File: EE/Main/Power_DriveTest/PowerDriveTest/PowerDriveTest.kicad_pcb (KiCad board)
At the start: 2 copper layers, 28.5 x 31 mm, 26 parts, among them J1 TAG_CONNECT, J2 Conn_01x02_Pin, J3 Conn_01x05_Pin, U1 LM3670MF-3.3, U2 SN74LVC1T45DBV, U3 STM32F030F4Px, U4 MCP1640Cx-xCHY

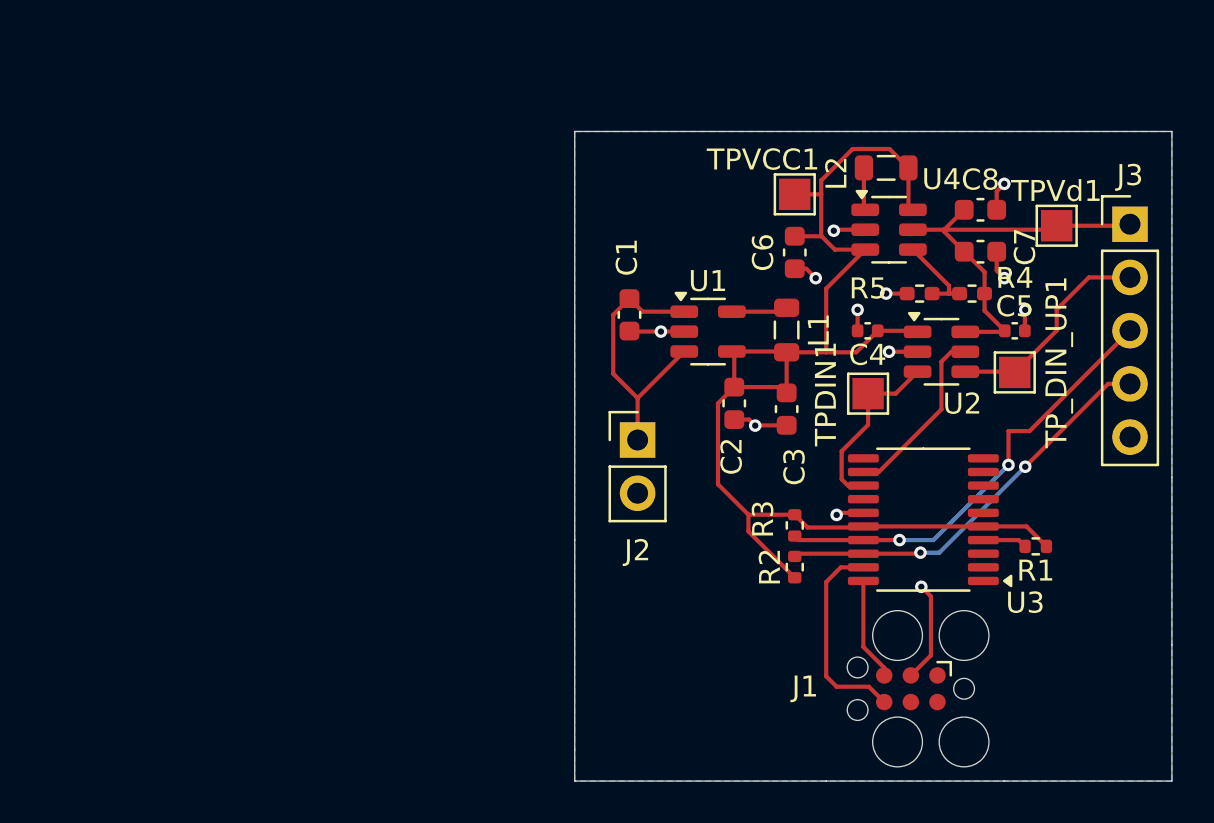
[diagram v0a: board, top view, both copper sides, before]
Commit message: New Power Board off to mfging
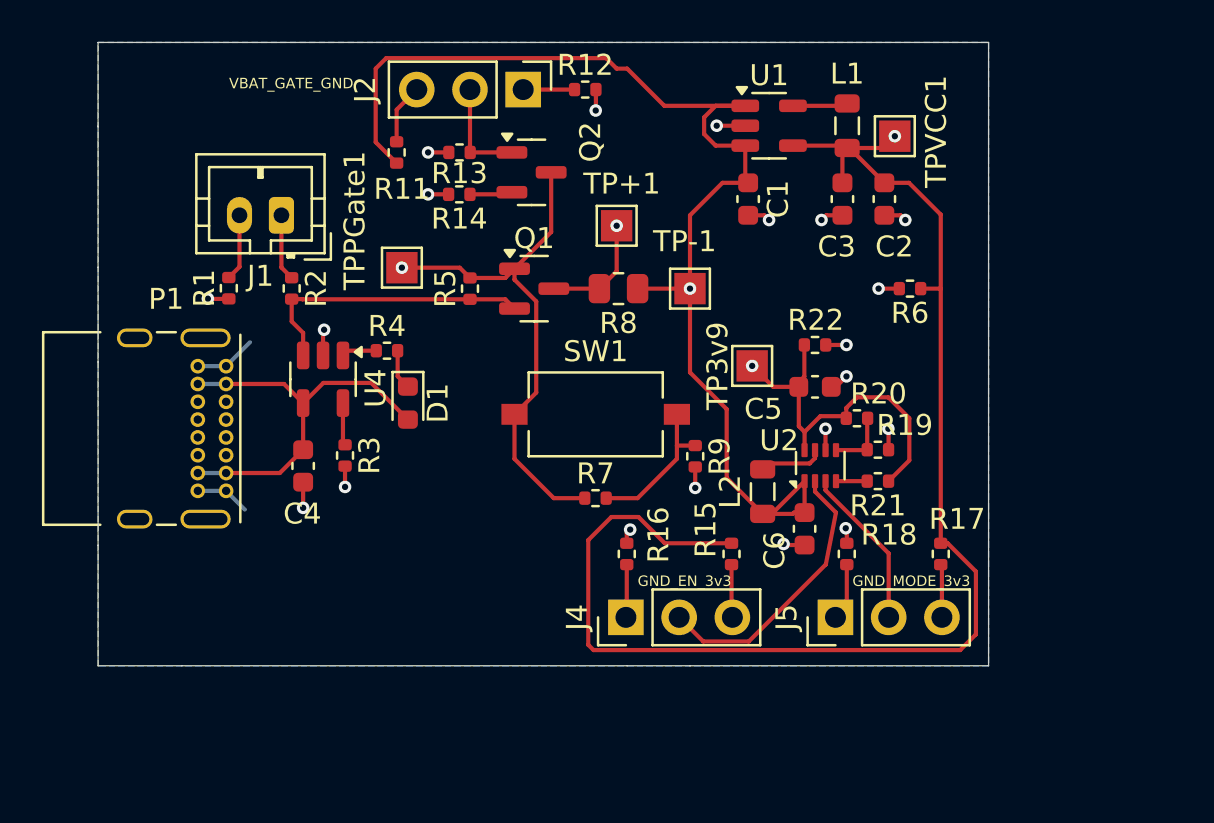
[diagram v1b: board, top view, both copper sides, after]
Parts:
- removed C7, C8: 4.7u, Capacitor_SMD:C_0603_1608Metric
- removed J3: Conn_01x05_Pin, Connector_PinHeader_2.54mm:PinHeader_1x05_P2.54mm_Vertical
- removed TPDIN1, TPVd1, TP_DIN_UP1: TestPoint, TestPoint:TestPoint_Pad_1.5x1.5mm
- removed U3: STM32F030F4Px, Package_SO:TSSOP-20_4.4x6.5mm_P0.65mm
- added D1: LED, LED_SMD:LED_0603_1608Metric, F.Cu at (148.0, 84.5)
- added J4: Conn_01x03_Pin, Connector_PinHeader_2.54mm:PinHeader_1x03_P2.54mm_Vertical, F.Cu at (158.4, 94.7)
- added J5: Conn_01x03_Pin, Connector_PinHeader_2.54mm:PinHeader_1x03_P2.54mm_Vertical, F.Cu at (168.4, 94.7)
- added P1: USB_C_Plug_USB2.0, Connector_USB:USB_C_Receptacle_GCT_USB4085, F.Cu at (139.4, 82.7)
- added Q1: Q_PMOS_GSD, Package_TO_SOT_SMD:SOT-23, F.Cu at (154.1, 79.0)
- added Q2: Q_NMOS_GSD, Package_TO_SOT_SMD:SOT-23, F.Cu at (153.9, 73.5)
- added R11: 10K, Resistor_SMD:R_0402_1005Metric, F.Cu at (147.5, 72.5)
- added R12: 10k, Resistor_SMD:R_0402_1005Metric, F.Cu at (156.5, 69.5)
- added R13: 10k, Resistor_SMD:R_0402_1005Metric, F.Cu at (150.5, 72.5)
- added R14: 10k, Resistor_SMD:R_0402_1005Metric, F.Cu at (150.5, 74.5)
- added R15: 10K, Resistor_SMD:R_0402_1005Metric, F.Cu at (163.5, 91.7)
- added R16: 10k, Resistor_SMD:R_0402_1005Metric, F.Cu at (158.5, 91.7)
- added R17: 10K, Resistor_SMD:R_0402_1005Metric, F.Cu at (173.5, 91.7)
- added R18: 10k, Resistor_SMD:R_0402_1005Metric, F.Cu at (169.0, 91.7)
- added R19: 100k, Resistor_SMD:R_0402_1005Metric, F.Cu at (170.5, 86.7)
- added R20: 550k, Resistor_SMD:R_0402_1005Metric, F.Cu at (169.5, 85.2)
- added R21: 10k, Resistor_SMD:R_0402_1005Metric, F.Cu at (170.5, 88.2)
- added R22: 1M, Resistor_SMD:R_0402_1005Metric, F.Cu at (167.5, 81.7)
- added R6: 1M, Resistor_SMD:R_0402_1005Metric, F.Cu at (172.0, 79.0)
- added R7: 0, Resistor_SMD:R_0402_1005Metric, F.Cu at (157.0, 89.0)
- added R8: 250m, Resistor_SMD:R_0805_2012Metric, F.Cu at (158.1, 79.0)
- added R9: 10k, Resistor_SMD:R_0402_1005Metric, F.Cu at (161.8, 87.0)
- added SW1: SW_SPST, Button_Switch_SMD:SW_Tactile_SPST_NO_Straight_CK_PTS636Sx25SMTRLFS, F.Cu at (157.0, 85.0)
- added TP+1: TestPoint, TestPoint:TestPoint_Pad_1.5x1.5mm, F.Cu at (158.0, 76.0)
- added TP-1: TestPoint, TestPoint:TestPoint_Pad_1.5x1.5mm, F.Cu at (161.5, 79.0)
- added TP3v9: TestPoint, TestPoint:TestPoint_Pad_1.5x1.5mm, F.Cu at (164.5, 82.7)
- added TPPGate1: TestPoint, TestPoint:TestPoint_Pad_1.5x1.5mm, F.Cu at (147.8, 78.0)
- C4, C5: value 0.1u -> 4.7u; footprint Capacitor_SMD:C_0402_1005Metric -> Capacitor_SMD:C_0603_1608Metric
- J1: value TAG_CONNECT -> Conn_01x02_Male; footprint Connector:Tag-Connect_TC2030-IDC-FP_2x03_P1.27mm_Vertical -> Connector_JST:JST_PH_B2B-PH-K_1x02_P2.00mm_Vertical
- J2: value Conn_01x02_Pin -> Conn_01x03_Pin; footprint Connector_PinHeader_2.54mm:PinHeader_1x02_P2.54mm_Vertical -> Connector_PinHeader_2.54mm:PinHeader_1x03_P2.54mm_Vertical
- L2: value 4.7u -> 0.47u
- R1: value 10k -> 0
- R2: value 4.7k -> 0
- R3: value 4.7k -> 10k
- R4: value 422k -> 2k; footprint Resistor_SMD:R_0402_1005Metric_Pad0.72x0.64mm_HandSolder -> Resistor_SMD:R_0402_1005Metric
- R5: value 250k -> 1M; footprint Resistor_SMD:R_0402_1005Metric_Pad0.72x0.64mm_HandSolder -> Resistor_SMD:R_0402_1005Metric
- U2: value SN74LVC1T45DBV -> ~; footprint Package_TO_SOT_SMD:SOT-23-6 -> Package_TO_SOT_SMD:SOT-583-8
- U4: value MCP1640Cx-xCHY -> MCP73832-2-OT; footprint Package_TO_SOT_SMD:SOT-23-6 -> Package_TO_SOT_SMD:SOT-23-5
- moved R1 40.4 mm to (139.5, 79.0), turned to 90 degrees
- moved J1 37.6 mm to (142.0, 75.5)
- moved R4 28.1 mm to (147.0, 82.0), turned to 0 degrees
- moved U4 27.9 mm to (144.0, 83.3), turned to -90 degrees
- moved C4 27.7 mm to (143.0, 87.5), turned to -90 degrees
- moved R2 27.4 mm to (142.5, 79.0), turned to -90 degrees
- moved R3 21.7 mm to (145.0, 87.0)
- moved R5 21.5 mm to (151.0, 79.0), turned to 90 degrees
- moved J2 17.6 mm to (153.5, 69.5), turned to -90 degrees
- moved L2 16.5 mm to (165.0, 88.7), turned to 90 degrees
- moved C6 13.2 mm to (167.0, 90.5), turned to 90 degrees
- moved C2 12.1 mm to (170.8, 74.7)
- moved C3 10.4 mm to (168.8, 74.7)
- moved U1 10.2 mm to (165.3, 71.2)
- moved L1 10.2 mm to (169.0, 71.2)
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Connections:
- C1 pad 1: /4v2 -> /VBAT_OUT
- C2 pad 1: VCC -> +3V3
- C3 pad 1: VCC -> +3V3
- C4 pad 1: VCC -> VBUS
- C5 pad 1: Vdrive -> /3v9
- C6 pad 1: VCC -> GND
- C6 pad 2: GND -> /VBAT_OUT
- J1 pad 1: unconnected-(J1-POWER_3V3-Pad1) -> Net-(J1-Pin_1)
- J1 pad 2: unconnected-(J1-UART_TX-Pad2) -> Net-(J1-Pin_2)
- J2 pad 1: /4v2 -> Net-(J2-Pin_1)
- J2 pad 2: GND -> /N_GATE
- L1 pad 2: VCC -> +3V3
- L2 pad 1: VCC -> /VBAT_OUT
- L2 pad 2: Net-(U4-SW) -> Net-(U2-SW)
- R1 pad 1: VCC -> GND
- R1 pad 2: Net-(U3-NRST) -> Net-(J1-Pin_2)
- R2 pad 1: VCC -> Net-(J1-Pin_1)
- R2 pad 2: /SDA -> /VBAT
- R3 pad 1: VCC -> Net-(U4-PROG)
- R3 pad 2: /SCL -> GND
- R4 pad 1: Vdrive -> Net-(U4-STAT)
- R4 pad 2: Net-(U4-V_{FB}) -> Net-(D1-K)
- R5 pad 1: Net-(U4-V_{FB}) -> /VBAT
- R5 pad 2: GND -> /GATE_EN
- TPVCC1 pad 1: VCC -> +3V3
- U1 pad 1: /4v2 -> /VBAT_OUT
- U1 pad 3: /4v2 -> /VBAT_OUT
- U1 pad 4: VCC -> +3V3
- U2 pad 1: VCC -> /VBAT_OUT
- U2 pad 2: GND -> /EN
- U2 pad 3: /DISPLAY_DIN -> /MODE
- U2 pad 4: /DISPLAY_DOUT -> Net-(U2-PG)
- U2 pad 5: /DIR -> Net-(U2-FB)
- U2 pad 6: Vdrive -> GND
- U4 pad 1: Net-(U4-SW) -> Net-(U4-STAT)
- U4 pad 3: VCC -> /VBAT
- U4 pad 4: Net-(U4-V_{FB}) -> VBUS
- U4 pad 5: Vdrive -> Net-(U4-PROG)
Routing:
- net +3V3: track 0.00 -> 66.3 mm, vias 0 -> 1
- net VCC: track 61.9 -> 0.00 mm
- net /VBAT_OUT: track 0.00 -> 58.5 mm, vias 0 -> 1
- net /GATE_EN: track 0.00 -> 25.2 mm, vias 0 -> 1
- net /SCL: track 21.2 -> 0.00 mm, vias 2 -> 0
- net Vdrive: track 19.7 -> 0.00 mm
- net /SDA: track 19.4 -> 0.00 mm, vias 2 -> 0
- net VBUS: track 0.00 -> 19.2 mm
- net /3v9: track 0.00 -> 17.8 mm, vias 0 -> 1
- net /VBAT: track 0.00 -> 13.8 mm
- net /4v2: track 13.6 -> 0.00 mm
- net /EN: track 0.00 -> 13.4 mm
- net /DISPLAY_DOUT: track 10.3 -> 0.00 mm
- net /SWDIO: track 9.84 -> 0.00 mm
- net /DIR: track 8.57 -> 0.00 mm
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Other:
- board size 28.5 x 31 mm -> 42.5 x 29.8 mm
- board text added: "GND_EN_3v3"
- board text added: "GND_MODE_3v3"
- board text added: "VBAT_GATE_GND"

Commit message: Placement Update
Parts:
- removed C3, C5: 4.7u, Capacitor_SMD:C_0603_1608Metric
- removed J1: Conn_01x02_Male, Connector_JST:JST_PH_B2B-PH-K_1x02_P2.00mm_Vertical
- removed J2, J4, J5: Conn_01x03_Pin, Connector_PinHeader_2.54mm:PinHeader_1x03_P2.54mm_Vertical
- removed L1: 4.7u, Inductor_SMD:L_0805_2012Metric
- removed R17: 10K, Resistor_SMD:R_0402_1005Metric
- removed R18, R21: 10k, Resistor_SMD:R_0402_1005Metric
- removed R19: 100k, Resistor_SMD:R_0402_1005Metric
- removed R22: 1M, Resistor_SMD:R_0402_1005Metric
- removed TP3v9: TestPoint, TestPoint:TestPoint_Pad_1.5x1.5mm
- removed U4: MCP73832-2-OT, Package_TO_SOT_SMD:SOT-23-5
- added C7: 0.1u, Capacitor_SMD:C_0402_1005Metric, F.Cu at (107.0, 101.3)
- added C8: 4.7u, Capacitor_SMD:C_0603_1608Metric, F.Cu at (121.6, 95.9)
- added C9: 0.1u, Capacitor_SMD:C_0402_1005Metric, F.Cu at (107.0, 103.2)
- added D2: LED, LED_SMD:LED_0603_1608Metric, F.Cu at (120.9, 79.0)
- added J7: TAG_CONNECT, Connector:Tag-Connect_TC2030-IDC-FP_2x03_P1.27mm_Vertical, F.Cu at (122.5, 24.9)
- added J8: Conn_01x02_Male, Connector_JST:JST_PH_B2B-PH-K_1x02_P2.00mm_Vertical, F.Cu at (100.6, 101.0)
- added Q3: Q_NMOS_GSD, Package_TO_SOT_SMD:SOT-23, F.Cu at (95.2, 86.8)
- added Q4: Q_NMOS_GSD, Package_TO_SOT_SMD:SOT-23, F.Cu at (95.2, 91.4)
- added R10: 10k, Resistor_SMD:R_0402_1005Metric_Pad0.72x0.64mm_HandSolder, F.Cu at (102.5, 82.1)
- added U3: 74LVC1GU04DRL, Package_TO_SOT_SMD:SOT-553, F.Cu at (121.1, 81.8)
- added U5: LM3670MF-3.3, Package_TO_SOT_SMD:TSOT-23-5, F.Cu at (120.9, 105.0)
- C1: value 4.7u -> 0.1u; footprint Capacitor_SMD:C_0603_1608Metric -> Capacitor_SMD:C_0402_1005Metric
- L2: value 0.47u -> 4.7u
- R1, R2: value 0 -> 100k; footprint Resistor_SMD:R_0402_1005Metric -> Resistor_SMD:R_0402_1005Metric_Pad0.72x0.64mm_HandSolder
- R11: value 10K -> 0; footprint Resistor_SMD:R_0402_1005Metric -> Resistor_SMD:R_0402_1005Metric_Pad0.72x0.64mm_HandSolder
- R12: value 10k -> 25m; footprint Resistor_SMD:R_0402_1005Metric -> Resistor_SMD:R_0805_2012Metric_Pad1.20x1.40mm_HandSolder
- R13, R9: value 10k -> 100k; footprint Resistor_SMD:R_0402_1005Metric -> Resistor_SMD:R_0402_1005Metric_Pad0.72x0.64mm_HandSolder
- R14, R15, R16, R3, R6, R7: footprint Resistor_SMD:R_0402_1005Metric -> Resistor_SMD:R_0402_1005Metric_Pad0.72x0.64mm_HandSolder
- R20: value 550k -> 4.7k; footprint Resistor_SMD:R_0402_1005Metric -> Resistor_SMD:R_0402_1005Metric_Pad0.72x0.64mm_HandSolder
- R4: value 2k -> 10k; footprint Resistor_SMD:R_0402_1005Metric -> Resistor_SMD:R_0402_1005Metric_Pad0.72x0.64mm_HandSolder
- R5: value 1M -> 4.7k; footprint Resistor_SMD:R_0402_1005Metric -> Resistor_SMD:R_0402_1005Metric_Pad0.72x0.64mm_HandSolder
- R8: value 250m -> 10; footprint Resistor_SMD:R_0805_2012Metric -> Resistor_SMD:R_0402_1005Metric_Pad0.72x0.64mm_HandSolder
- SW1: value SW_SPST -> SW_DPST; footprint Button_Switch_SMD:SW_Tactile_SPST_NO_Straight_CK_PTS636Sx25SMTRLFS -> Library:401-1133-ND
- U1: value LM3670MF-3.3 -> STM32G431K6Tx; footprint Package_TO_SOT_SMD:TSOT-23-5 -> Package_QFP:LQFP-32_7x7mm_P0.8mm
- U2: value ~ -> MCP73832-2-OT; footprint Package_TO_SOT_SMD:SOT-583-8 -> Package_TO_SOT_SMD:SOT-23-5
- moved TPVCC1 84.1 mm to (94.5, 106.1)
- moved R6 73.1 mm to (99.3, 86.1), turned to 0 degrees
- moved TP-1 69.9 mm to (94.5, 99.0), turned to 0 degrees
- moved R12 67.4 mm to (100.0, 106.3)
- moved TP+1 66.4 mm to (94.5, 95.4), turned to 0 degrees
- moved R20 63.7 mm to (105.8, 82.1)
- moved C1 62.3 mm to (107.0, 99.3), turned to 0 degrees
- moved U1 61.4 mm to (116.3, 34.2)
- moved R9 59.6 mm to (102.5, 80.1), turned to 0 degrees
- moved Q2 59.4 mm to (95.2, 82.2)
- moved R15 59.2 mm to (105.8, 78.2), turned to 0 degrees
- moved Q1 58.9 mm to (95.2, 77.6)
- moved TPPGate1 58.6 mm to (94.5, 102.5)
- moved P1 56.3 mm to (97.5, 45.0)
- moved R7 55.9 mm to (102.5, 76.2)
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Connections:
- C1 pad 1: /VBAT_OUT -> +3V3
- C2 pad 1: +3V3 -> VBUS
- C4 pad 1: VBUS -> /VBAT_OUT
- C6 pad 1: GND -> +3V3
- C6 pad 2: /VBAT_OUT -> GND
- L2 pad 1: /VBAT_OUT -> Net-(U5-SW)
- L2 pad 2: Net-(U2-SW) -> +3V3
- P1 pad S1: unconnected-(P1-SHIELD-PadS1) -> GND
- Q1 pad 1: /GATE_EN -> Net-(Q1-G)
- Q2 pad 1: /N_GATE -> Net-(Q2-G)
- Q2 pad 3: /GATE_EN -> Net-(Q1-G)
- R1 pad 1: GND -> /VBAT_OUT
- R1 pad 2: Net-(J1-Pin_2) -> /EN
- R11 pad 1: /VBAT_OUT -> Net-(J8-Pin_1)
- R11 pad 2: Net-(J2-Pin_3) -> /VBAT
- R12 pad 1: Net-(J2-Pin_1) -> /VBAT_OUT
- R12 pad 2: GND -> /P_DRAIN
- R13 pad 1: /N_GATE -> Net-(Q2-G)
- R15 pad 2: Net-(J4-Pin_3) -> Net-(Q2-G)
- R16 pad 1: Net-(J4-Pin_1) -> +3V3
- R16 pad 2: GND -> Net-(U1-PG10)
- R2 pad 1: Net-(J1-Pin_1) -> /KillPower
- R2 pad 2: /VBAT -> GND
- R20 pad 1: /3v9 -> GND
- R20 pad 2: Net-(U2-FB) -> Net-(D2-K)
- R3 pad 1: Net-(U4-PROG) -> Net-(U1-PB8)
- R4 pad 1: Net-(U4-STAT) -> Net-(U2-PROG)
- R4 pad 2: Net-(D1-K) -> GND
- R5 pad 1: /VBAT -> Net-(U2-STAT)
- R5 pad 2: /GATE_EN -> Net-(D1-K)
- R6 pad 1: +3V3 -> /VBAT
- R6 pad 2: GND -> Net-(Q1-G)
- R7 pad 1: /GATE_EN -> /N_GATE
- R7 pad 2: Net-(SW1-B) -> Net-(Q2-G)
- R8 pad 1: /VBAT_OUT -> +3V3
- R8 pad 2: /P_DRAIN -> Net-(Q4-D)
- R9 pad 1: Net-(SW1-B) -> /KillPower
- SW1 pad 1: /GATE_EN -> +3V3
- SW1 pad 2: Net-(SW1-B) -> /BTN_SNS
- TPPGate1 pad 1: /GATE_EN -> Net-(Q1-G)
- U1 pad 1: /VBAT_OUT -> +3V3
- U1 pad 2: GND -> unconnected-(U1-PF0-Pad2)
- U1 pad 3: /VBAT_OUT -> unconnected-(U1-PF1-Pad3)
- U1 pad 4: +3V3 -> Net-(U1-PG10)
- U1 pad 5: Net-(U1-SW) -> unconnected-(U1-PA0-Pad5)
- U2 pad 1: /VBAT_OUT -> Net-(U2-STAT)
- U2 pad 2: /EN -> GND
- U2 pad 3: /MODE -> /VBAT
- U2 pad 4: Net-(U2-PG) -> VBUS
- U2 pad 5: Net-(U2-FB) -> Net-(U2-PROG)
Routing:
- net +3V3: track 66.3 -> 0.00 mm, vias 1 -> 0
- net /VBAT_OUT: track 58.5 -> 0.00 mm, vias 1 -> 0
- net GND: track 26.1 -> 0.00 mm, vias 20 -> 0
- net /GATE_EN: track 25.2 -> 0.00 mm, vias 1 -> 0
- net VBUS: track 19.2 -> 0.00 mm
- net /3v9: track 17.8 -> 0.00 mm, vias 1 -> 0
- net /VBAT: track 13.8 -> 0.00 mm
- net /EN: track 13.4 -> 0.00 mm
- net /MODE: track 7.75 -> 0.00 mm
- net Net-(SW1-B): track 7.16 -> 0.00 mm
- net /P_DRAIN: track 5.52 -> 0.00 mm, vias 1 -> 0
- net /N_GATE: track 4.99 -> 0.00 mm
- net Net-(J1-Pin_1): track 3.18 -> 0.00 mm
- net Net-(J1-Pin_2): track 3.18 -> 0.00 mm
- net Net-(U2-SW): track 3.10 -> 0.00 mm
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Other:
- board outline removed
- board text removed: "GND_EN_3v3"
- board text removed: "GND_MODE_3v3"
- board text removed: "VBAT_GATE_GND"

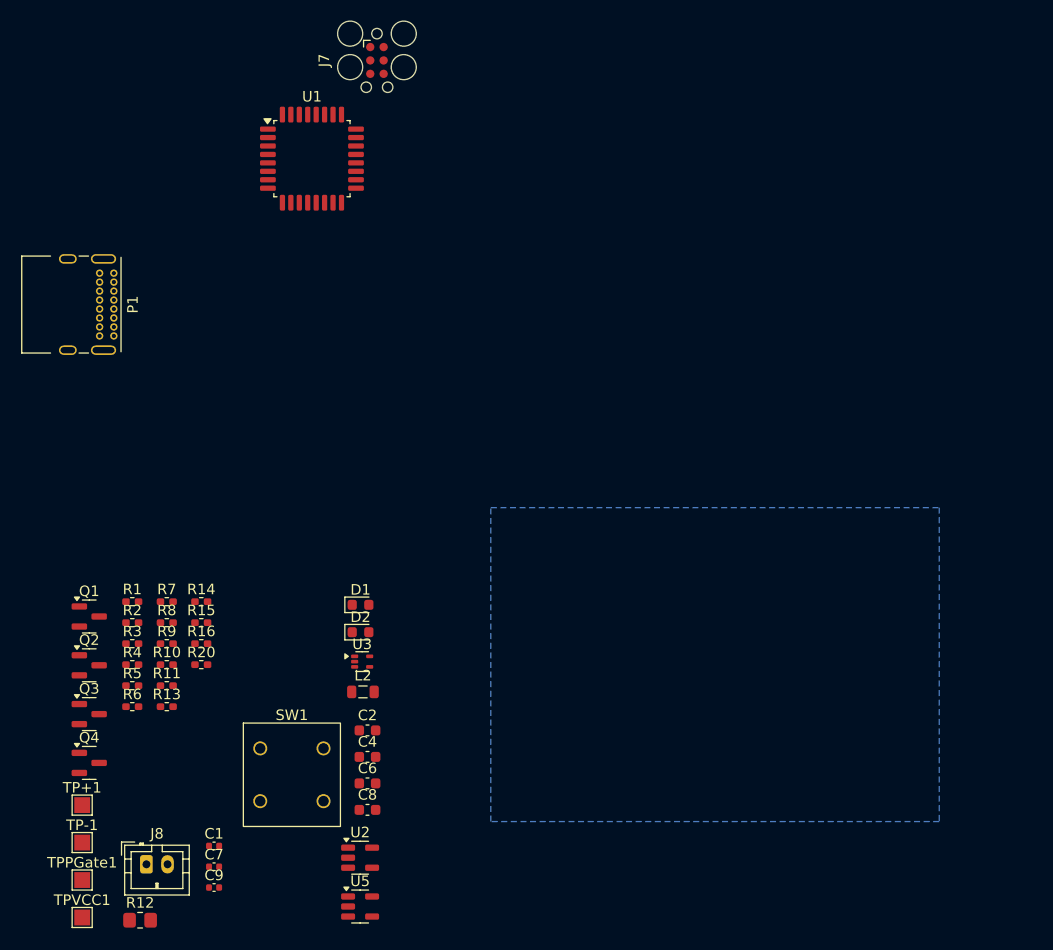
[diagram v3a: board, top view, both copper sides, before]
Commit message: Adding Test Circuit 2
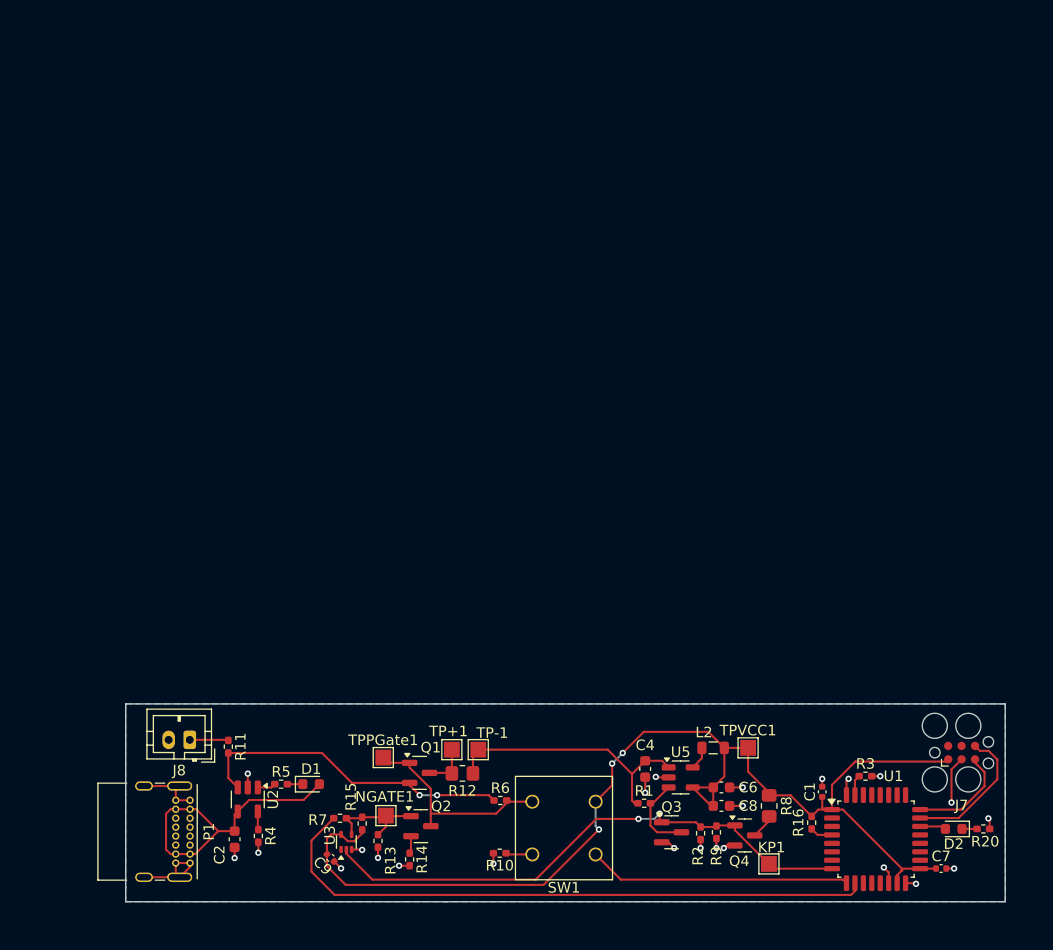
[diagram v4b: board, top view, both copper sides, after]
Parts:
- added KP1: TestPoint, TestPoint:TestPoint_Pad_1.5x1.5mm, F.Cu at (159.6, 101.0)
- added NGATE1: TestPoint, TestPoint:TestPoint_Pad_1.5x1.5mm, F.Cu at (123.3, 96.4)
- R8: footprint Resistor_SMD:R_0402_1005Metric_Pad0.72x0.64mm_HandSolder -> Resistor_SMD:R_0805_2012Metric_Pad1.20x1.40mm_HandSolder
- moved J7 85.9 mm to (177.9, 90.5), turned to 0 degrees
- moved U1 83.8 mm to (169.8, 98.7)
- moved R20 75.7 mm to (179.9, 97.7), turned to 180 degrees
- moved R3 70.6 mm to (168.8, 92.7)
- moved C7 68.9 mm to (175.9, 101.4)
- moved TPVCC1 65.1 mm to (157.6, 90.0)
- moved Q4 62.5 mm to (157.3, 98.3)
- moved R16 60.3 mm to (163.7, 97.1), turned to -90 degrees
- moved R8 59.7 mm to (159.6, 95.5), turned to -90 degrees
- moved D2 59.2 mm to (177.1, 97.7), turned to 180 degrees
- moved C1 57.9 mm to (164.7, 94.2), turned to 90 degrees
- moved R2 57.4 mm to (153.1, 98.1), turned to -90 degrees
- moved Q3 56.3 mm to (150.4, 98.0)
- moved R9 55.1 mm to (154.6, 98.0), turned to -90 degrees
- moved R1 52.1 mm to (147.8, 95.3)
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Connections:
- J7 pad 1: VCC -> +3V3
- U1 pad 10: unconnected-(U1-PA5-Pad10) -> /N_GATE
- U1 pad 12: /KillPower -> unconnected-(U1-PA7-Pad12)
- U1 pad 18: /N_GATE -> unconnected-(U1-PA8-Pad18)
- U1 pad 22: unconnected-(U1-PA12-Pad22) -> /HB
- U1 pad 26: /HB -> unconnected-(U1-PB3-Pad26)
- U1 pad 8: unconnected-(U1-PA3-Pad8) -> /KillPower
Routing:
- net +3V3: track 0.00 -> 110.7 mm, vias 0 -> 3
- net /N_GATE: track 0.00 -> 59.3 mm
- net /KillPower: track 0.00 -> 52.9 mm, vias 0 -> 2
- net GND: track 0.00 -> 44.2 mm, vias 0 -> 24
- net /VBAT: track 0.00 -> 30.8 mm, vias 0 -> 2
- net VBUS: track 0.00 -> 27.7 mm
- net /VBAT_OUT: track 0.00 -> 25.4 mm
- net /BTN_SNS: track 0.00 -> 24.9 mm
- net Net-(Q1-G): track 0.00 -> 19.9 mm
- net /SWDIO: track 0.00 -> 13.4 mm
- net Net-(Q2-G): track 0.00 -> 10.6 mm
- net /SWDCLK: track 0.00 -> 9.95 mm
- net /EN: track 0.00 -> 7.66 mm
- net /P_DRAIN: track 0.00 -> 4.40 mm
- net Net-(J8-Pin_1): track 0.00 -> 3.67 mm
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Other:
- board outline added: 83.3 x 18.8 mm
